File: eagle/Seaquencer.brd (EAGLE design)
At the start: 94.9 x 72.4 mm, 52 parts, among them IC1 ATMEGA48/88/168, IC2 74HC595N

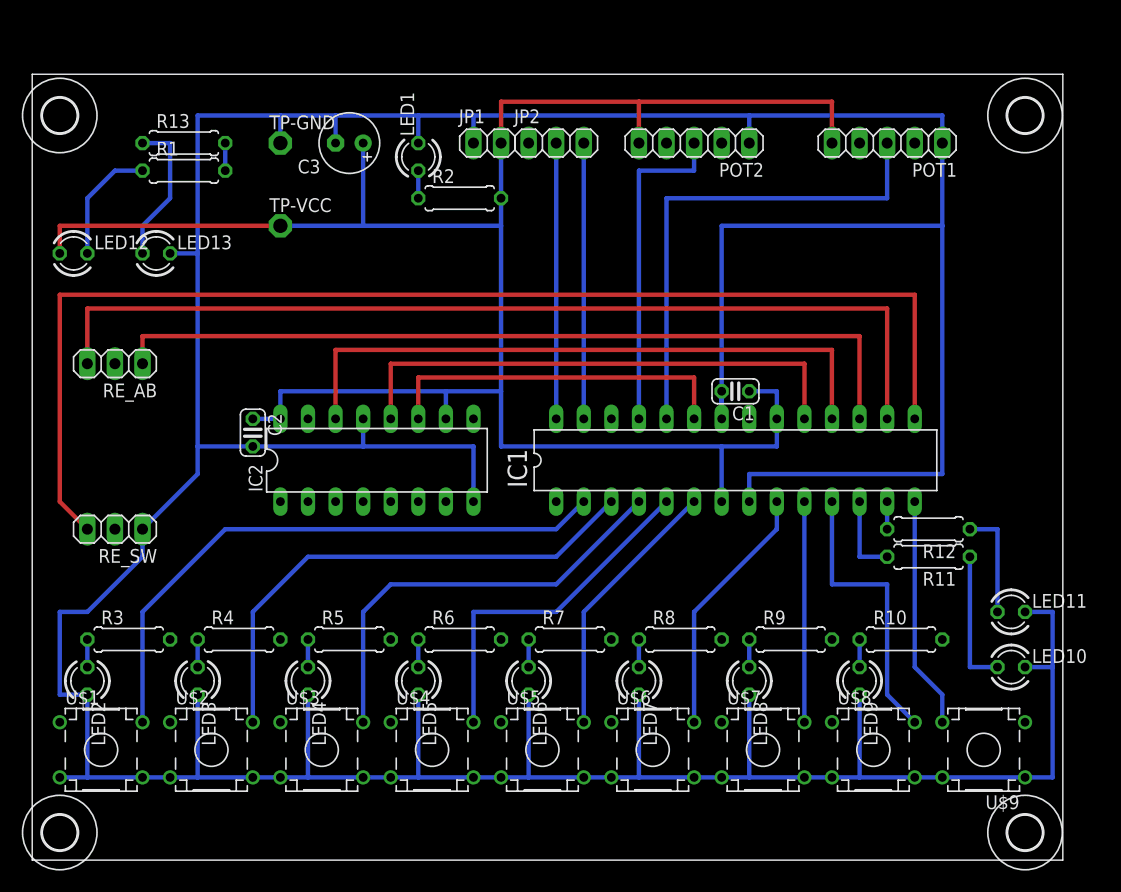
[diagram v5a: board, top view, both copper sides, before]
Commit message: Sequencer.brd: Rotary Encoder付近のLEDの位置を変更
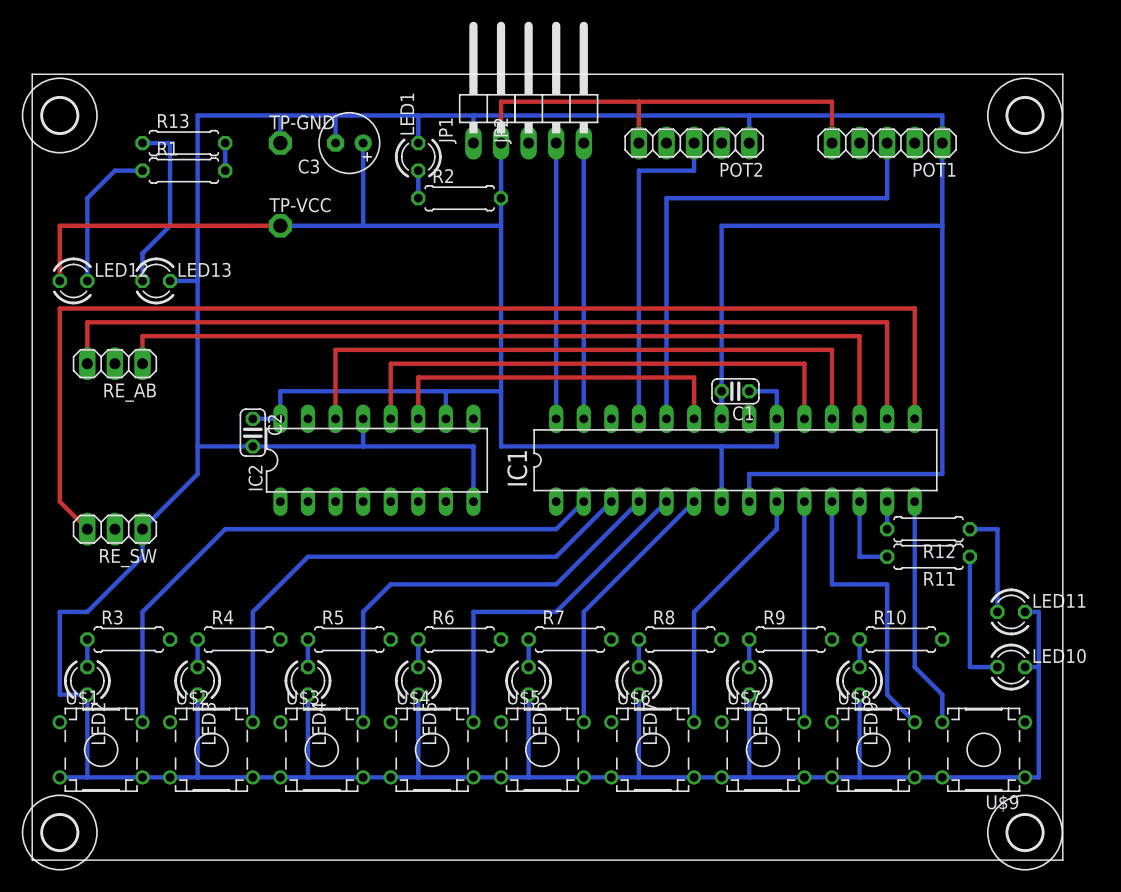
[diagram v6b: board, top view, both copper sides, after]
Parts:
- JP1: device pinhead:1X02 -> pinhead:1X02/90
- JP2: device pinhead:1X03 -> pinhead:1X03/90
- moved JP1 3.81 mm to (41.9, 69.8)
- moved JP2 3.81 mm to (48.3, 69.8)
- moved LED12 2.54 mm to (3.81, 53.3)
- moved LED13 2.54 mm to (11.4, 53.3)
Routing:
- net GND: track 446.2 -> 442.4 mm
- net +3V3: track 186.7 -> 189.2 mm
- net RE_S: track 112.8 -> 110.3 mm
- net N$37: track 13.8 -> 16.3 mm
- net N$32: track 11.2 -> 13.8 mm
- net RE_A: track 88.9 -> 86.4 mm
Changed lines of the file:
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@@
 <element name="U$7" library="mylib" package="TME1" value="AK_TCTSW" x="67.31" y="10.16" rot="R270"/>
 <element name="U$8" library="mylib" package="TME1" value="AK_TCTSW" x="77.47" y="10.16" rot="R270"/>
-<element name="JP1" library="pinhead" package="1X02" value="3.3VIN" x="41.91" y="66.04"/>
+<element name="JP1" library="pinhead" package="1X02/90" value="3.3VIN" x="41.91" y="69.85"/>
 <element name="IC2" library="74xx-eu" package="DIL16" value="74HC595N" x="31.75" y="36.83"/>
 <element name="R2" library="rcl" package="0207/7" value="2k" x="39.37" y="60.96"/>
@@
 <element name="RE_AB" library="pinhead" package="1X03" value="" x="7.62" y="45.72" rot="R180"/>
 <element name="RE_SW" library="pinhead" package="1X03" value="" x="7.62" y="30.48" rot="R180"/>
-<element name="JP2" library="pinhead" package="1X03" value="I2C" x="48.26" y="66.04"/>
+<element name="JP2" library="pinhead" package="1X03/90" value="I2C" x="48.26" y="69.85"/>
 <element name="POT1" library="pinhead" package="1X05" value="" x="78.74" y="66.04" rot="R180"/>
 <element name="POT2" library="pinhead" package="1X05" value="" x="60.96" y="66.04" rot="R180"/>
-<element name="LED12" library="led" package="LED3MM" value="" x="3.81" y="55.88"/>
+<element name="LED12" library="led" package="LED3MM" value="" x="3.81" y="53.34"/>
 <element name="R1" library="rcl" package="0207/7" value="2k" x="13.97" y="63.5"/>
-<element name="LED13" library="led" package="LED3MM" value="" x="11.43" y="55.88"/>
+<element name="LED13" library="led" package="LED3MM" value="" x="11.43" y="53.34"/>
 <element name="R13" library="rcl" package="0207/7" value="1.5k" x="13.97" y="66.04"/>
 <element name="C3" library="rcl" package="E2,5-6" value="47uF" x="29.21" y="66.04" rot="R180"/>
@@
 <contactref element="RE_SW" pad="1"/>
 <wire x1="20.32" y1="38.1" x2="15.24" y2="38.1" width="0.4064" layer="16"/>
-<wire x1="15.24" y1="38.1" x2="15.24" y2="55.88" width="0.4064" layer="16"/>
-<wire x1="15.24" y1="55.88" x2="15.24" y2="68.58" width="0.4064" layer="16"/>
+<wire x1="15.24" y1="38.1" x2="15.24" y2="53.34" width="0.4064" layer="16"/>
+<wire x1="15.24" y1="53.34" x2="15.24" y2="68.58" width="0.4064" layer="16"/>
 <wire x1="2.54" y1="15.24" x2="5.08" y2="15.24" width="0.4064" layer="16"/>
 <wire x1="15.24" y1="68.58" x2="22.86" y2="68.58" width="0.4064" layer="16"/>
@@
 <wire x1="66.04" y1="66.04" x2="66.04" y2="68.58" width="0.4064" layer="16"/>
 <contactref element="LED13" pad="K"/>
-<wire x1="12.7" y1="55.88" x2="15.24" y2="55.88" width="0.4064" layer="16"/>
+<wire x1="12.7" y1="53.34" x2="15.24" y2="53.34" width="0.4064" layer="16"/>
 <wire x1="2.54" y1="22.86" x2="2.54" y2="15.24" width="0.4064" layer="16"/>
 <wire x1="15.24" y1="35.56" x2="15.24" y2="38.1" width="0.4064" layer="16"/>
@@
 <wire x1="66.04" y1="35.56" x2="83.82" y2="35.56" width="0.4064" layer="16"/>
 <wire x1="83.82" y1="35.56" x2="83.82" y2="58.42" width="0.4064" layer="16"/>
-<wire x1="91.44" y1="7.62" x2="93.98" y2="7.62" width="0.4064" layer="16"/>
-<wire x1="93.98" y1="7.62" x2="93.98" y2="17.78" width="0.4064" layer="16"/>
-<wire x1="93.98" y1="17.78" x2="93.98" y2="22.86" width="0.4064" layer="16"/>
-<wire x1="93.98" y1="22.86" x2="91.44" y2="22.86" width="0.4064" layer="16"/>
-<wire x1="91.44" y1="17.78" x2="93.98" y2="17.78" width="0.4064" layer="16"/>
+<wire x1="91.44" y1="7.62" x2="92.71" y2="7.62" width="0.4064" layer="16"/>
+<wire x1="92.71" y1="7.62" x2="92.71" y2="17.78" width="0.4064" layer="16"/>
+<wire x1="92.71" y1="17.78" x2="92.71" y2="22.86" width="0.4064" layer="16"/>
+<wire x1="92.71" y1="22.86" x2="91.44" y2="22.86" width="0.4064" layer="16"/>
+<wire x1="91.44" y1="17.78" x2="92.71" y2="17.78" width="0.4064" layer="16"/>
 <wire x1="40.64" y1="33.02" x2="40.64" y2="38.1" width="0.4064" layer="16"/>
 <wire x1="40.64" y1="38.1" x2="30.48" y2="38.1" width="0.4064" layer="16"/>
@@
 <wire x1="22.86" y1="58.42" x2="30.48" y2="58.42" width="0.4064" layer="16"/>
 <wire x1="30.48" y1="58.42" x2="43.18" y2="58.42" width="0.4064" layer="16"/>
-<wire x1="2.54" y1="55.88" x2="2.54" y2="58.42" width="0.4064" layer="1"/>
+<wire x1="2.54" y1="53.34" x2="2.54" y2="58.42" width="0.4064" layer="1"/>
 <wire x1="2.54" y1="58.42" x2="22.86" y2="58.42" width="0.4064" layer="1"/>
 <contactref element="IC1" pad="20"/>
@@
 <contactref element="RE_AB" pad="3"/>
 <contactref element="IC1" pad="16"/>
-<wire x1="78.74" y1="40.64" x2="78.74" y2="50.8" width="0.4064" layer="1"/>
-<wire x1="78.74" y1="50.8" x2="5.08" y2="50.8" width="0.4064" layer="1"/>
-<wire x1="5.08" y1="50.8" x2="5.08" y2="45.72" width="0.4064" layer="1"/>
+<wire x1="78.74" y1="40.64" x2="78.74" y2="49.53" width="0.4064" layer="1"/>
+<wire x1="78.74" y1="49.53" x2="5.08" y2="49.53" width="0.4064" layer="1"/>
+<wire x1="5.08" y1="49.53" x2="5.08" y2="45.72" width="0.4064" layer="1"/>
 </signal>
 <signal name="N$41">
@@
 <contactref element="RE_SW" pad="3"/>
 <contactref element="IC1" pad="15"/>
-<wire x1="81.28" y1="40.64" x2="81.28" y2="52.07" width="0.4064" layer="1"/>
-<wire x1="81.28" y1="52.07" x2="2.54" y2="52.07" width="0.4064" layer="1"/>
-<wire x1="2.54" y1="52.07" x2="2.54" y2="33.02" width="0.4064" layer="1"/>
+<wire x1="81.28" y1="40.64" x2="81.28" y2="50.8" width="0.4064" layer="1"/>
+<wire x1="81.28" y1="50.8" x2="2.54" y2="50.8" width="0.4064" layer="1"/>
+<wire x1="2.54" y1="50.8" x2="2.54" y2="33.02" width="0.4064" layer="1"/>
 <wire x1="2.54" y1="33.02" x2="5.08" y2="30.48" width="0.4064" layer="1"/>
 </signal>
@@
 <wire x1="10.16" y1="63.5" x2="7.62" y2="63.5" width="0.4064" layer="16"/>
 <wire x1="7.62" y1="63.5" x2="5.08" y2="60.96" width="0.4064" layer="16"/>
-<wire x1="5.08" y1="60.96" x2="5.08" y2="55.88" width="0.4064" layer="16"/>
+<wire x1="5.08" y1="60.96" x2="5.08" y2="53.34" width="0.4064" layer="16"/>
 </signal>
 <signal name="N$37">
 <contactref element="LED13" pad="A"/>
 <contactref element="R13" pad="1"/>
-<wire x1="12.7" y1="60.96" x2="12.7" y2="66.04" width="0.4064" layer="16"/>
+<wire x1="12.7" y1="58.42" x2="12.7" y2="66.04" width="0.4064" layer="16"/>
 <wire x1="12.7" y1="66.04" x2="10.16" y2="66.04" width="0.4064" layer="16"/>
-<wire x1="10.16" y1="55.88" x2="10.16" y2="58.42" width="0.4064" layer="16"/>
-<wire x1="10.16" y1="58.42" x2="12.7" y2="60.96" width="0.4064" layer="16"/>
+<wire x1="10.16" y1="53.34" x2="10.16" y2="55.88" width="0.4064" layer="16"/>
+<wire x1="10.16" y1="55.88" x2="12.7" y2="58.42" width="0.4064" layer="16"/>
 </signal>
 </signals>
